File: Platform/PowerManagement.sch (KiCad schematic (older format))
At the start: 17 parts, among them J1 12V INPUT, J2 12V_INPUT, J3 Barrel_Jack, U1 LM7805_TO220, U2 LM317_TO-220

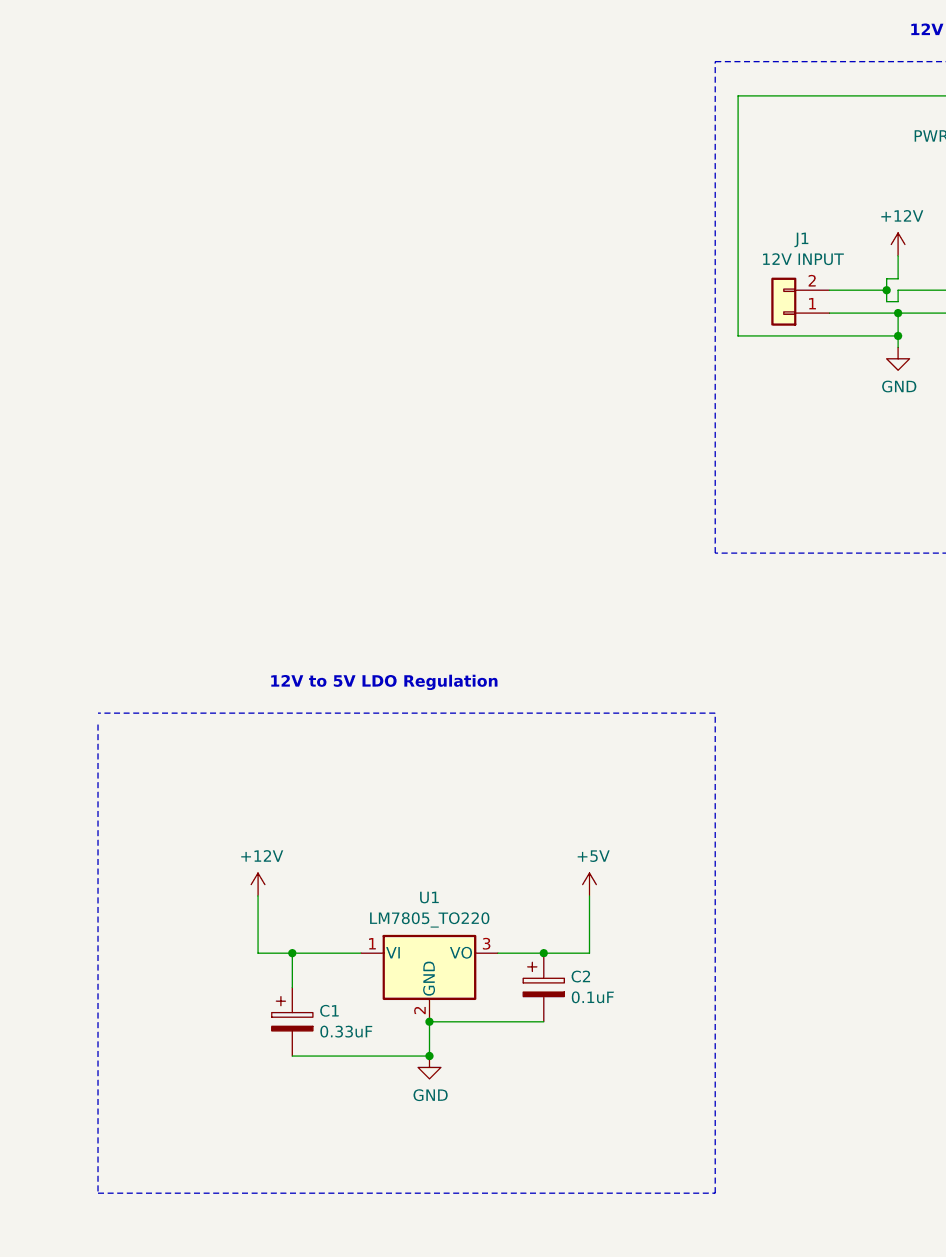
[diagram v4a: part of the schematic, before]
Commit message: updated platform schematic.
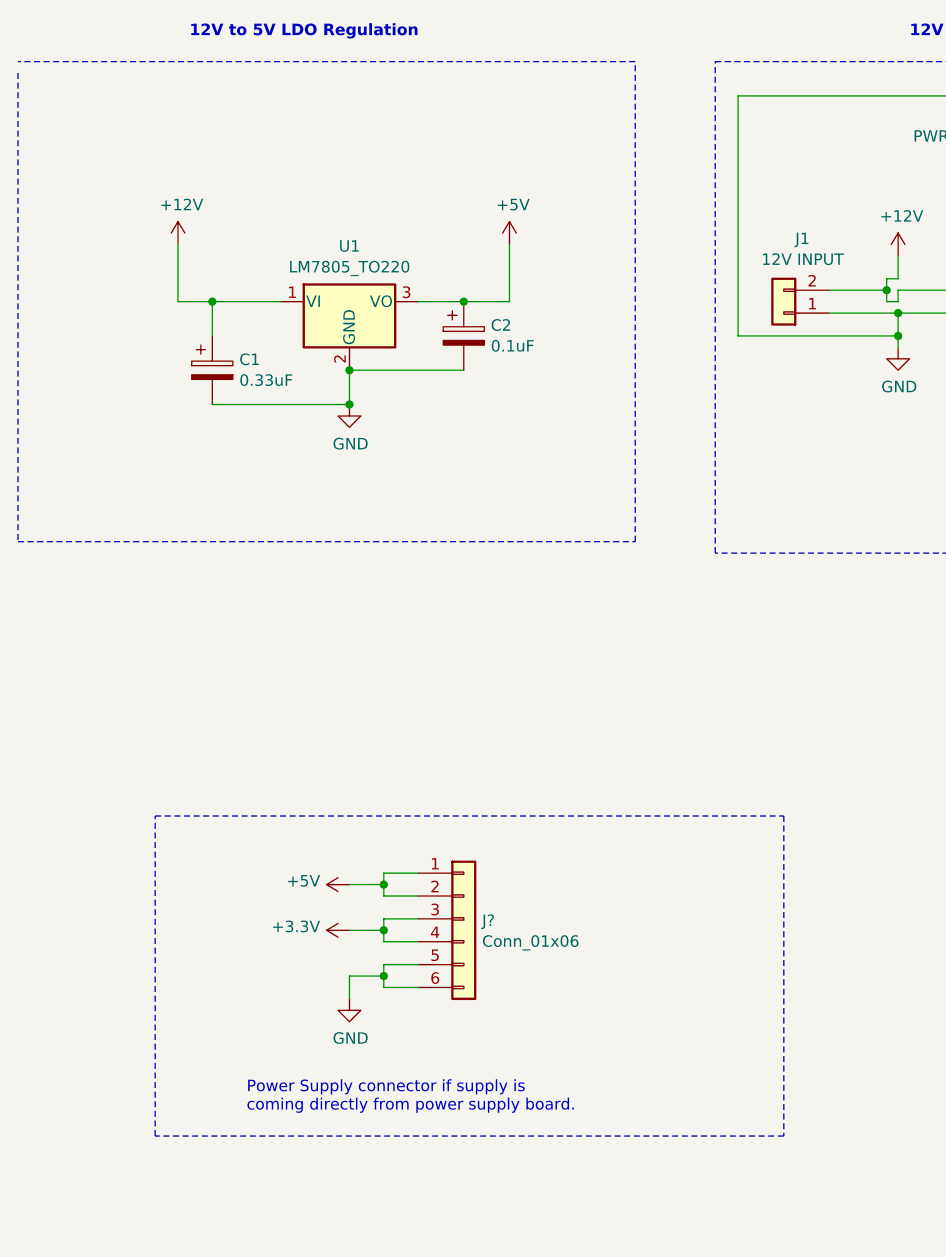
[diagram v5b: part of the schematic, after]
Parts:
- added J?: Conn_01x06, symbol Connector_Generic:Conn_01x06
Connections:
- net +3V3: now also J?.3 (Pin_3), J?.4 (Pin_4)
- net +5V: now also J?.1 (Pin_1), J?.2 (Pin_2)
- net GND: now also J?.5 (Pin_5), J?.6 (Pin_6)
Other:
- note added: "Power Supply connector if supply is\ncoming directly from power supply board."
- moved on the sheet: C1, C2, U1
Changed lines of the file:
@@
 L Regulator_Linear:LM7805_TO220 U1
 U 1 1 5FA72B80
-P 3100 4800
-F 0 "U1" H 3100 5042 50  0000 C CNN
-F 1 "LM7805_TO220" H 3100 4951 50  0000 C CNN
-F 2 "Package_TO_SOT_THT:TO-220-3_Vertical" H 3100 5025 50  0001 C CIN
-F 3 "https://www.onsemi.cn/PowerSolutions/document/MC7800-D.PDF" H 3100 4750 50  0001 C CNN
-	1    3100 4800
+P 2750 1950
+F 0 "U1" H 2750 2192 50  0000 C CNN
+F 1 "LM7805_TO220" H 2750 2101 50  0000 C CNN
+F 2 "Package_TO_SOT_THT:TO-220-3_Vertical" H 2750 2175 50  0001 C CIN
+F 3 "https://www.onsemi.cn/PowerSolutions/document/MC7800-D.PDF" H 2750 1900 50  0001 C CNN
+	1    2750 1950
 	1    0    0    -1
 $EndComp
@@
 L power:+12V #PWR01
 U 1 1 5FA73447
-P 2350 4550
-F 0 "#PWR01" H 2350 4400 50  0001 C CNN
-F 1 "+12V" H 2365 4723 50  0000 C CNN
-F 2 "" H 2350 4550 50  0001 C CNN
-F 3 "" H 2350 4550 50  0001 C CNN
-	1    2350 4550
-	1    0    0    -1
-$EndComp
-Wire Wire Line
-	2350 4550 2350 4800
-Wire Wire Line
-	2350 4800 2500 4800
+P 2000 1700
+F 0 "#PWR01" H 2000 1550 50  0001 C CNN
+F 1 "+12V" H 2015 1873 50  0000 C CNN
+F 2 "" H 2000 1700 50  0001 C CNN
+F 3 "" H 2000 1700 50  0001 C CNN
+	1    2000 1700
+	1    0    0    -1
+$EndComp
+Wire Wire Line
+	2000 1700 2000 1950
+Wire Wire Line
+	2000 1950 2150 1950
 $Comp
 L power:+5V #PWR03
 U 1 1 5FA73B37
-P 3800 4550
-F 0 "#PWR03" H 3800 4400 50  0001 C CNN
-F 1 "+5V" H 3815 4723 50  0000 C CNN
-F 2 "" H 3800 4550 50  0001 C CNN
-F 3 "" H 3800 4550 50  0001 C CNN
-	1    3800 4550
-	1    0    0    -1
-$EndComp
-Wire Wire Line
-	3800 4550 3800 4800
-Wire Wire Line
-	3800 4800 3600 4800
+P 3450 1700
+F 0 "#PWR03" H 3450 1550 50  0001 C CNN
+F 1 "+5V" H 3465 1873 50  0000 C CNN
+F 2 "" H 3450 1700 50  0001 C CNN
+F 3 "" H 3450 1700 50  0001 C CNN
+	1    3450 1700
+	1    0    0    -1
+$EndComp
+Wire Wire Line
+	3450 1700 3450 1950
+Wire Wire Line
+	3450 1950 3250 1950
 $Comp
 L power:GND #PWR02
 U 1 1 5FA74A2F
-P 3100 5250
-F 0 "#PWR02" H 3100 5000 50  0001 C CNN
-F 1 "GND" H 3105 5077 50  0000 C CNN
-F 2 "" H 3100 5250 50  0001 C CNN
-F 3 "" H 3100 5250 50  0001 C CNN
-	1    3100 5250
-	1    0    0    -1
-$EndComp
-Wire Wire Line
-	3100 5250 3100 5100
+P 2750 2400
+F 0 "#PWR02" H 2750 2150 50  0001 C CNN
+F 1 "GND" H 2755 2227 50  0000 C CNN
+F 2 "" H 2750 2400 50  0001 C CNN
+F 3 "" H 2750 2400 50  0001 C CNN
+	1    2750 2400
+	1    0    0    -1
+$EndComp
+Wire Wire Line
+	2750 2400 2750 2250
 $Comp
 L Device:CP C1
 U 1 1 5FA7541C
-P 2500 5100
-F 0 "C1" H 2618 5146 50  0000 L CNN
-F 1 "0.33uF" H 2618 5055 50  0000 L CNN
-F 2 "" H 2538 4950 50  0001 C CNN
-F 3 "~" H 2500 5100 50  0001 C CNN
-	1    2500 5100
-	1    0    0    -1
-$EndComp
-Wire Wire Line
-	2500 4950 2500 4800
-Connection ~ 2500 4800
-Wire Wire Line
-	2500 4800 2800 4800
-Wire Wire Line
-	2500 5250 3100 5250
-Connection ~ 3100 5250
+P 2150 2250
+F 0 "C1" H 2268 2296 50  0000 L CNN
+F 1 "0.33uF" H 2268 2205 50  0000 L CNN
+F 2 "" H 2188 2100 50  0001 C CNN
+F 3 "~" H 2150 2250 50  0001 C CNN
+	1    2150 2250
+	1    0    0    -1
+$EndComp
+Wire Wire Line
+	2150 2100 2150 1950
+Connection ~ 2150 1950
+Wire Wire Line
+	2150 1950 2450 1950
+Wire Wire Line
+	2150 2400 2750 2400
+Connection ~ 2750 2400
 $Comp
 L Device:CP C2
 U 1 1 5FA75BDB
-P 3600 4950
-F 0 "C2" H 3718 4996 50  0000 L CNN
-F 1 "0.1uF" H 3718 4905 50  0000 L CNN
-F 2 "" H 3638 4800 50  0001 C CNN
-F 3 "~" H 3600 4950 50  0001 C CNN
-	1    3600 4950
-	1    0    0    -1
-$EndComp
-Connection ~ 3600 4800
-Wire Wire Line
-	3600 4800 3400 4800
-Wire Wire Line
-	3600 5100 3100 5100
-Connection ~ 3100 5100
+P 3250 2100
+F 0 "C2" H 3368 2146 50  0000 L CNN
+F 1 "0.1uF" H 3368 2055 50  0000 L CNN
+F 2 "" H 3288 1950 50  0001 C CNN
+F 3 "~" H 3250 2100 50  0001 C CNN
+	1    3250 2100
+	1    0    0    -1
+$EndComp
+Connection ~ 3250 1950
+Wire Wire Line
+	3250 1950 3050 1950
+Wire Wire Line
+	3250 2250 2750 2250
+Connection ~ 2750 2250
 $Comp
 L Platform-rescue:LM317_TO-220-Regulator_Linear-Platform-rescue U2
@@
 	10150 3450 10150 6050
 Wire Notes Line
-	1650 3800 1650 5850
-Wire Notes Line
-	1650 5850 4350 5850
-Wire Notes Line
-	4350 5850 4350 3750
-Wire Notes Line
-	4350 3750 1650 3750
+	1300 950  1300 3000
+Wire Notes Line
+	1300 3000 4000 3000
+Wire Notes Line
+	4000 3000 4000 900
+Wire Notes Line
+	4000 900  1300 900
 Text Notes 5200 800  0    50   ~ 10
 12V Input Connector
-Text Notes 2400 3650 0    50   ~ 10
+Text Notes 2050 800  0    50   ~ 10
 12V to 5V LDO Regulation
 Text Notes 7150 3350 0    50   ~ 10
@@
 Wire Wire Line
 	5150 2000 6000 2000
+$Comp
+L Connector_Generic:Conn_01x06 J?
+U 1 1 60174FE6
+P 3250 4650
+F 0 "J?" H 3330 4642 50  0000 L CNN
+F 1 "Conn_01x06" H 3330 4551 50  0000 L CNN
+F 2 "" H 3250 4650 50  0001 C CNN
+F 3 "~" H 3250 4650 50  0001 C CNN
+	1    3250 4650
+	1    0    0    -1
+$EndComp
+Wire Wire Line
+	3050 4450 2900 4450
+Wire Wire Line
+	2900 4450 2900 4500
+Wire Wire Line
+	2900 4550 3050 4550
+Wire Wire Line
+	3050 4650 2900 4650
+Wire Wire Line
+	2900 4750 3050 4750
+Wire Wire Line
+	3050 4850 2900 4850
+Wire Wire Line
+	2900 4850 2900 4900
+Wire Wire Line
+	2900 4950 3050 4950
+$Comp
+L power:GND #PWR?
+U 1 1 60179FD7
+P 2750 5000
+F 0 "#PWR?" H 2750 4750 50  0001 C CNN
+F 1 "GND" H 2755 4827 50  0000 C CNN
+F 2 "" H 2750 5000 50  0001 C CNN
+F 3 "" H 2750 5000 50  0001 C CNN
+	1    2750 5000
+	1    0    0    -1
+$EndComp
+Wire Wire Line
+	2750 5000 2750 4900
+Wire Wire Line
+	2750 4900 2900 4900
+Connection ~ 2900 4900
+Wire Wire Line
+	2900 4900 2900 4950
+$Comp
+L power:+5V #PWR?
+U 1 1 6017E3B0
+P 2750 4500
+F 0 "#PWR?" H 2750 4350 50  0001 C CNN
+F 1 "+5V" V 2765 4628 50  0000 L CNN
+F 2 "" H 2750 4500 50  0001 C CNN
+F 3 "" H 2750 4500 50  0001 C CNN
+	1    2750 4500
+	0    -1   -1   0
+$EndComp
+Wire Wire Line
+	2750 4500 2900 4500
+Connection ~ 2900 4500
+Wire Wire Line
+	2900 4500 2900 4550
+Wire Wire Line
+	2900 4650 2900 4700
+$Comp
+L power:+3.3V #PWR?
+U 1 1 6018128A
+P 2750 4700
+F 0 "#PWR?" H 2750 4550 50  0001 C CNN
+F 1 "+3.3V" V 2765 4828 50  0000 L CNN
+F 2 "" H 2750 4700 50  0001 C CNN
+F 3 "" H 2750 4700 50  0001 C CNN
+	1    2750 4700
+	0    -1   -1   0
+$EndComp
+Wire Wire Line
+	2750 4700 2900 4700
+Connection ~ 2900 4700
+Wire Wire Line
+	2900 4700 2900 4750
+Wire Notes Line
+	4650 4200 4650 5600
+Wire Notes Line
+	4650 5600 1900 5600
+Wire Notes Line
+	1900 5600 1900 4200
+Wire Notes Line
+	1900 4200 4650 4200
+Text Notes 2300 5500 0    50   ~ 0
+Power Supply connector if supply is\ncoming directly from power supply board.
 $EndSCHEMATC

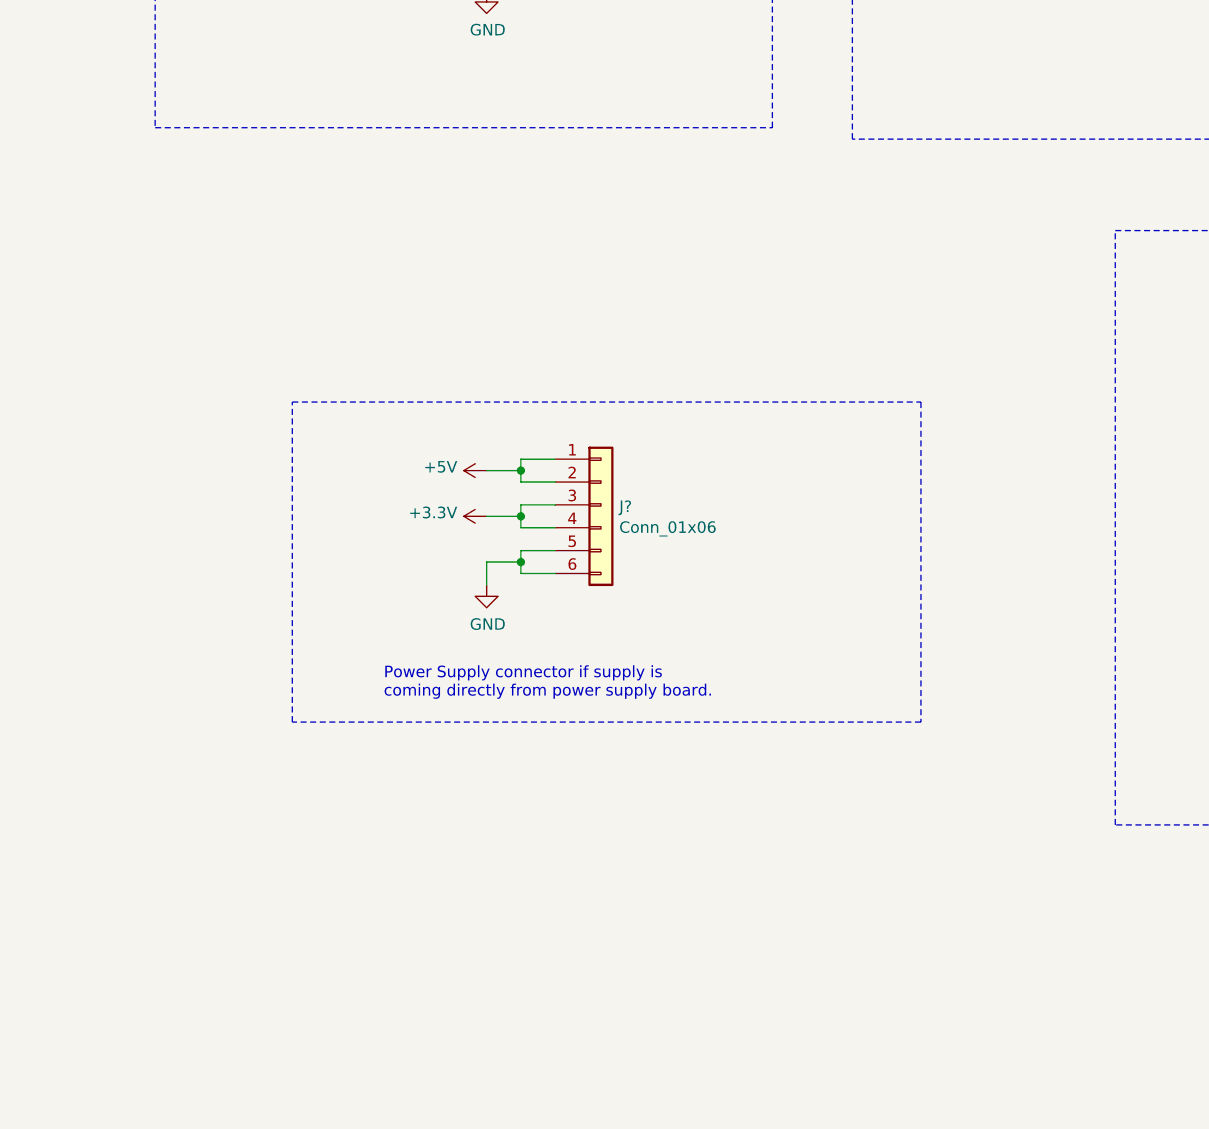
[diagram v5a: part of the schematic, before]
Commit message: updated the schematic as per the latest IO xls.
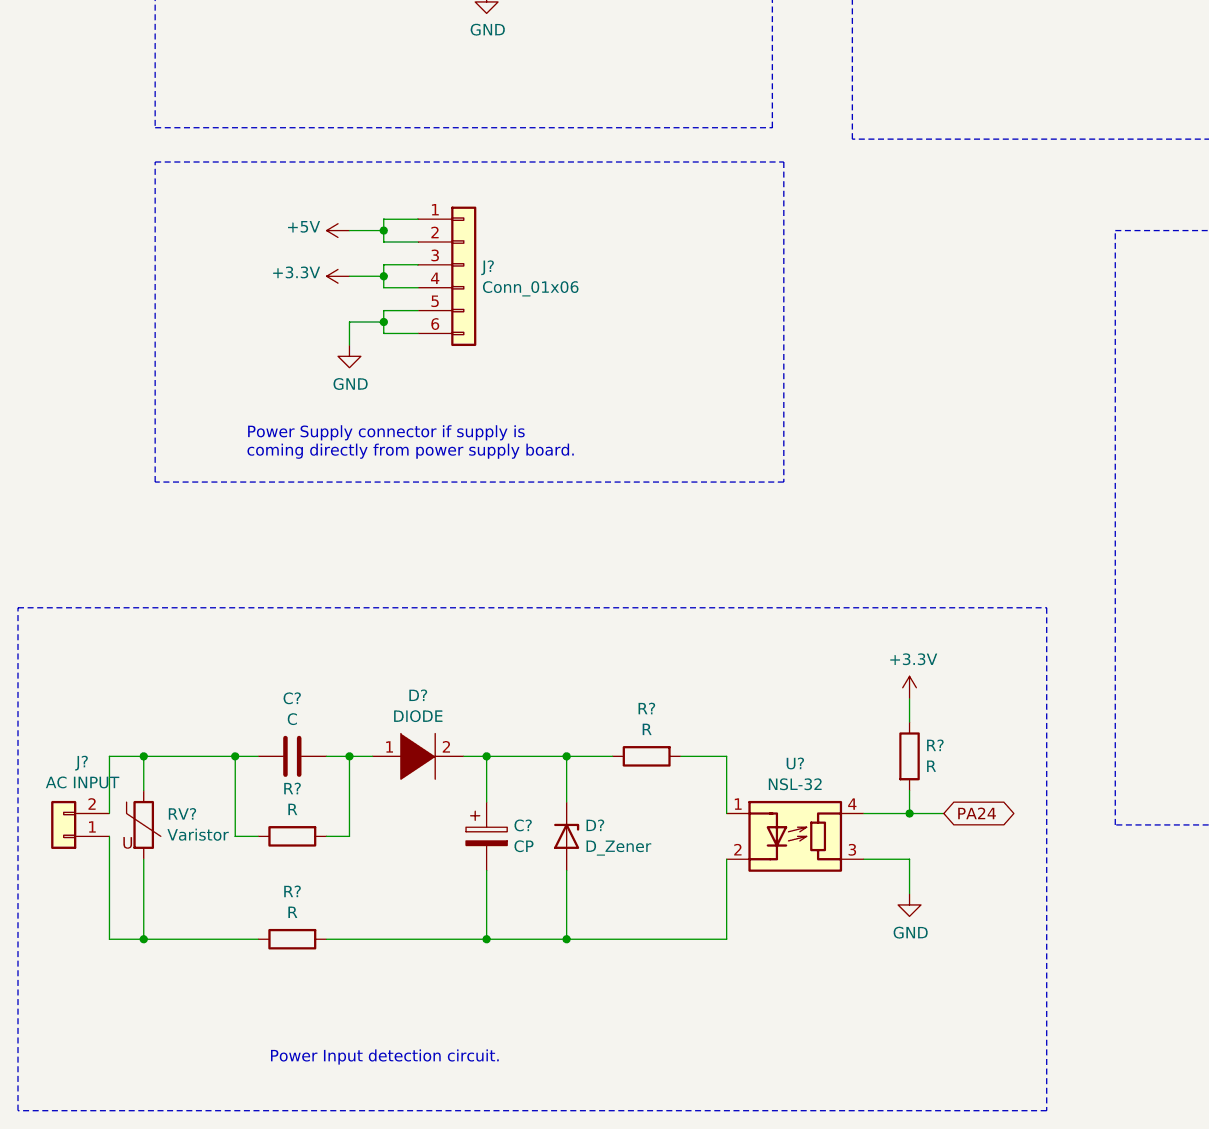
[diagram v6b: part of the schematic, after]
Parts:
- added C?: C, symbol Device:C
- added C?: CP, symbol Device:CP
- added D?: DIODE, symbol pspice:DIODE
- added D?: D_Zener, symbol Device:D_Zener
- added J?: AC INPUT, symbol Connector_Generic:Conn_01x02
- added R? (x4): R, symbol Device:R
- added RV?: Varistor, symbol Device:Varistor
- added U?: NSL-32, OptoDevice:Luna_NSL-32, symbol Isolator:NSL-32
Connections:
- net +3V3: now also R?.1
- net GND: now also U?.3 (R)
- new net: J?.1 (Pin_1), R?.1, RV?.2
- new net: C?.1, J?.2 (Pin_2), R?.1, RV?.1
- new net: C?.2, D?.1 (K), R?.2
- new net: C?.2, D?.2 (A), R?.2, U?.2 (K)
- new net: C?.1, D?.1 (K), D?.2 (A), R?.1
- new net: R?.2, U?.1 (A)
- new net PA24: R?.2, U?.4 (R)
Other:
- note added: "Power Input detection circuit."
- moved on the sheet: J?
